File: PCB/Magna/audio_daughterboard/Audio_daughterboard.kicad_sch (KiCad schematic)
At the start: 41 parts, among them J101 Conn_02x15_Odd_Even, U101 CY2305SXC-1HT, U102 CY2305SXC-1HT

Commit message: Update schematics to Kicad 9
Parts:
- U101: LCSC C914887 -> CY2305
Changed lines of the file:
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@@
 	(wire
 		(pts
-			(xy 59.69 74.93) (xy 83.82 74.93)
+			(xy 196.85 71.12) (xy 196.85 90.17)
 		)
 		(stroke
@@
 	(wire
 		(pts
-			(xy 196.85 71.12) (xy 196.85 90.17)
+			(xy 176.53 82.55) (xy 234.95 82.55)
 		)
 		(stroke
@@
 	(wire
 		(pts
-			(xy 176.53 82.55) (xy 234.95 82.55)
+			(xy 288.29 257.81) (xy 288.29 260.35)
 		)
 		(stroke
@@
 	(wire
 		(pts
-			(xy 288.29 257.81) (xy 288.29 260.35)
+			(xy 87.63 52.07) (xy 59.69 52.07)
 		)
 		(stroke
@@
 	(wire
 		(pts
-			(xy 87.63 52.07) (xy 59.69 52.07)
+			(xy 293.37 210.82) (xy 344.17 210.82)
 		)
 		(stroke
@@
 	(wire
 		(pts
-			(xy 293.37 210.82) (xy 344.17 210.82)
+			(xy 379.73 30.48) (xy 379.73 81.28)
 		)
 		(stroke
@@
 	(wire
 		(pts
-			(xy 379.73 30.48) (xy 379.73 81.28)
+			(xy 163.83 74.93) (xy 163.83 77.47)
 		)
 		(stroke
@@
 	(wire
 		(pts
-			(xy 163.83 74.93) (xy 163.83 77.47)
+			(xy 59.69 74.93) (xy 83.82 74.93)
 		)
 		(stroke
@@
 					(size 1.27 1.27)
 				)
+				(hide yes)
 			)
 		)
@@
 					(size 1.27 1.27)
 				)
+				(hide yes)
 			)
 		)
@@
 					(size 1.27 1.27)
 				)
+				(hide yes)
 			)
 		)
@@
 					(size 1.27 1.27)
 				)
+				(hide yes)
 			)
 		)
@@
 					(size 1.27 1.27)
 				)
+				(hide yes)
 			)
 		)
@@
 					(size 1.27 1.27)
 				)
+				(hide yes)
 			)
 		)
@@
 					(size 1.27 1.27)
 				)
+				(hide yes)
 			)
 		)
@@
 					(size 1.27 1.27)
 				)
+				(hide yes)
 			)
 		)
@@
 					(size 1.27 1.27)
 				)
+				(hide yes)
 			)
 		)
@@
 					(size 1.27 1.27)
 				)
+				(hide yes)
 			)
 		)
@@
 					(size 1.27 1.27)
 				)
+				(hide yes)
 			)
 		)
@@
 					(size 1.27 1.27)
 				)
+				(hide yes)
 			)
 		)
@@
 					(size 1.27 1.27)
 				)
+				(hide yes)
 			)
 		)
@@
 					(size 1.27 1.27)
 				)
+				(hide yes)
 			)
 		)
@@
 					(size 1.27 1.27)
 				)
+				(hide yes)
 			)
 		)
@@
 					(size 1.27 1.27)
 				)
+				(hide yes)
 			)
 		)
@@
 					(size 1.27 1.27)
 				)
+				(hide yes)
 			)
 		)
@@
 					(size 1.27 1.27)
 				)
+				(hide yes)
 			)
 		)
@@
 					(size 1.27 1.27)
 				)
+				(hide yes)
 			)
 		)
@@
 					(size 1.27 1.27)
 				)
+				(hide yes)
 			)
 		)
@@
 					(size 1.27 1.27)
 				)
+				(hide yes)
 			)
 		)
@@
 					(size 1.27 1.27)
 				)
+				(hide yes)
 			)
 		)
@@
 					(size 1.27 1.27)
 				)
+				(hide yes)
 			)
 		)
@@
 					(size 1.27 1.27)
 				)
+				(hide yes)
 			)
 		)
@@
 					(size 1.27 1.27)
 				)
+				(hide yes)
 			)
 		)
@@
 					(size 1.27 1.27)
 				)
+				(hide yes)
 			)
 		)
@@
 					(size 1.27 1.27)
 				)
+				(hide yes)
 			)
 		)
@@
 					(size 1.27 1.27)
 				)
+				(hide yes)
 			)
 		)
@@
 					(size 1.27 1.27)
 				)
+				(hide yes)
 			)
 		)
@@
 					(size 1.27 1.27)
 				)
+				(hide yes)
 			)
 		)
@@
 					(size 1.27 1.27)
 				)
+				(hide yes)
 			)
 		)
@@
 					(size 1.27 1.27)
 				)
+				(hide yes)
 			)
 		)
@@
 					(size 1.27 1.27)
 				)
+				(hide yes)
 			)
 		)
@@
 					(size 1.27 1.27)
 				)
+				(hide yes)
 			)
 		)
@@
 					(size 1.27 1.27)
 				)
+				(hide yes)
 			)
 		)
@@
 					(size 1.27 1.27)
 				)
+				(hide yes)
 			)
 		)
@@
 					(size 1.27 1.27)
 				)
+				(hide yes)
 			)
 		)
@@
 					(size 1.27 1.27)
 				)
+				(hide yes)
 			)
 		)
@@
 					(size 1.27 1.27)
 				)
+				(hide yes)
 			)
 		)
@@
 					(size 1.27 1.27)
 				)
+				(hide yes)
 			)
 		)
@@
 					(size 1.27 1.27)
 				)
+				(hide yes)
 			)
 		)
@@
 					(size 1.27 1.27)
 				)
+				(hide yes)
 			)
 		)
@@
 					(size 1.27 1.27)
 				)
+				(hide yes)
 			)
 		)
@@
 					(size 1.27 1.27)
 				)
+				(hide yes)
 			)
 		)
@@
 					(size 1.27 1.27)
 				)
+				(hide yes)
 			)
 		)
@@
 					(size 1.27 1.27)
 				)
+				(hide yes)
 			)
 		)
@@
 					(size 1.27 1.27)
 				)
+				(hide yes)
 			)
 		)
@@
 					(size 1.27 1.27)
 				)
+				(hide yes)
 			)
 		)
@@
 					(size 1.27 1.27)
 				)
+				(hide yes)
 			)
 		)
@@
 					(size 1.27 1.27)
 				)
+				(hide yes)
 			)
 		)
@@
 					(size 1.27 1.27)
 				)
+				(hide yes)
 			)
 		)
@@
 					(size 1.27 1.27)
 				)
+				(hide yes)
 			)
 		)
@@
 					(size 1.27 1.27)
 				)
+				(hide yes)
 			)
 		)
@@
 					(size 1.27 1.27)
 				)
+				(hide yes)
 			)
 		)
@@
 					(size 1.27 1.27)
 				)
+				(hide yes)
 			)
 		)
@@
 					(size 1.27 1.27)
 				)
+				(hide yes)
 			)
 		)
@@
 					(size 1.27 1.27)
 				)
+				(hide yes)
 			)
 		)
@@
 					(size 1.27 1.27)
 				)
+				(hide yes)
 			)
 		)
@@
 					(size 1.27 1.27)
 				)
+				(hide yes)
 			)
 		)
@@
 		(at 163.83 87.63 0)
 		(unit 1)
-		(exclude_from_sim yes)
+		(exclude_from_sim no)
 		(in_bom yes)
 		(on_board yes)
@@
 		(fields_autoplaced yes)
 		(property "Reference" "U101"
-			(at 165.8494 76.361 0)
+			(at 165.9733 75.9163 0)
 			(effects
 				(font
@@
 		)
 		(property "Value" "CY2305SXC-1HT"
-			(at 165.8494 78.8979 0)
+			(at 165.9733 78.3406 0)
 			(effects
 				(font
@@
 		)
 		(property "Footprint" "Package_SO:SOIC-8_3.9x4.9mm_P1.27mm"
-			(at 163.83 87.63 0)
+			(at 163.83 85.09 0)
 			(effects
 				(font
@@
 		)
 		(property "Datasheet" "https://datasheet.lcsc.com/lcsc/2011101039_Cypress-Semicon-CY2305SXC-1HT_C914887.pdf"
-			(at 163.83 87.63 0)
+			(at 163.83 90.17 0)
 			(effects
 				(font
@@
 					(size 1.27 1.27)
 				)
+				(hide yes)
 			)
 		)
-		(property "LCSC" "C914887"
+		(property "LCSC" "CY2305"
 			(at 163.83 87.63 0)
 			(effects
@@
 					(size 1.27 1.27)
 				)
+				(hide yes)
 			)
 		)
@@
 					(size 1.27 1.27)
 				)
+				(hide yes)
 			)
 		)

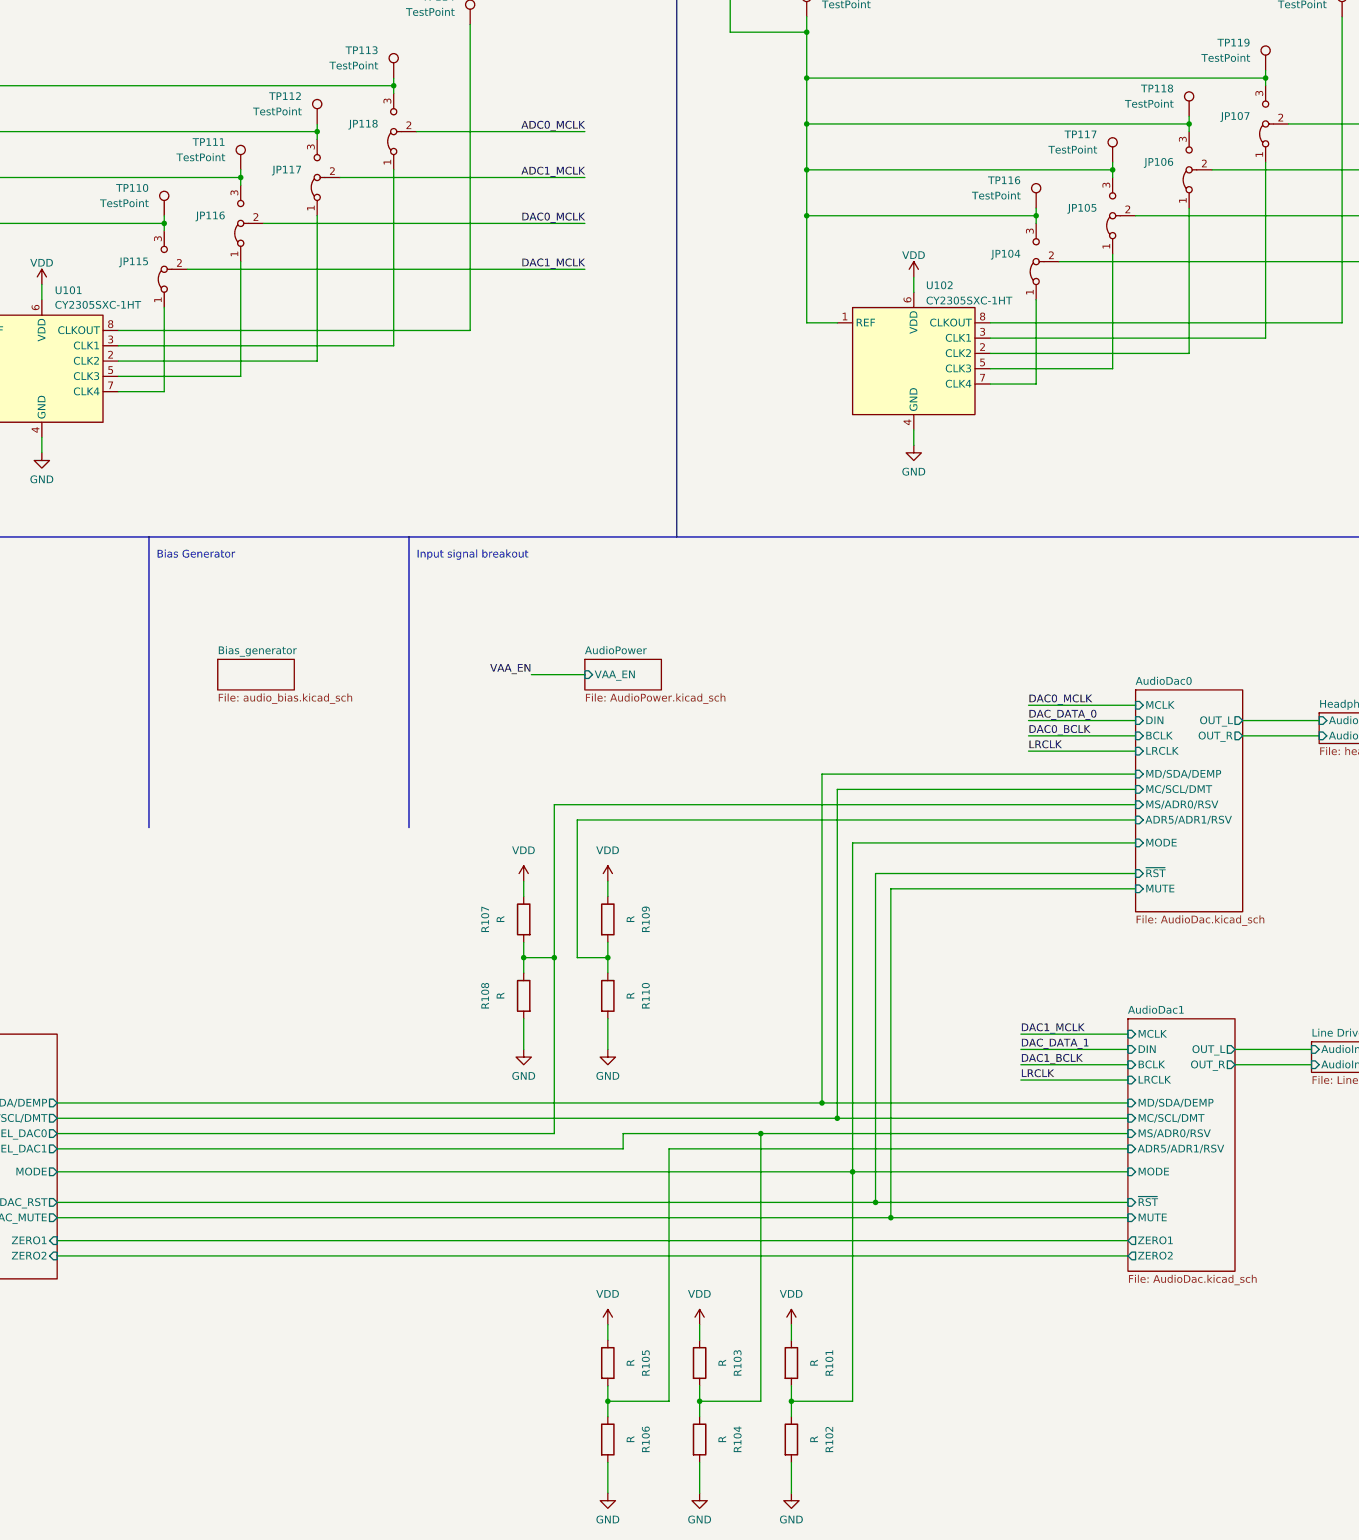
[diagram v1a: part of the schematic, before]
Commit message: Update audio PCB
Mainly added simulations to Linedriver and DAC.

Also fixed some small issues that was found when simulating
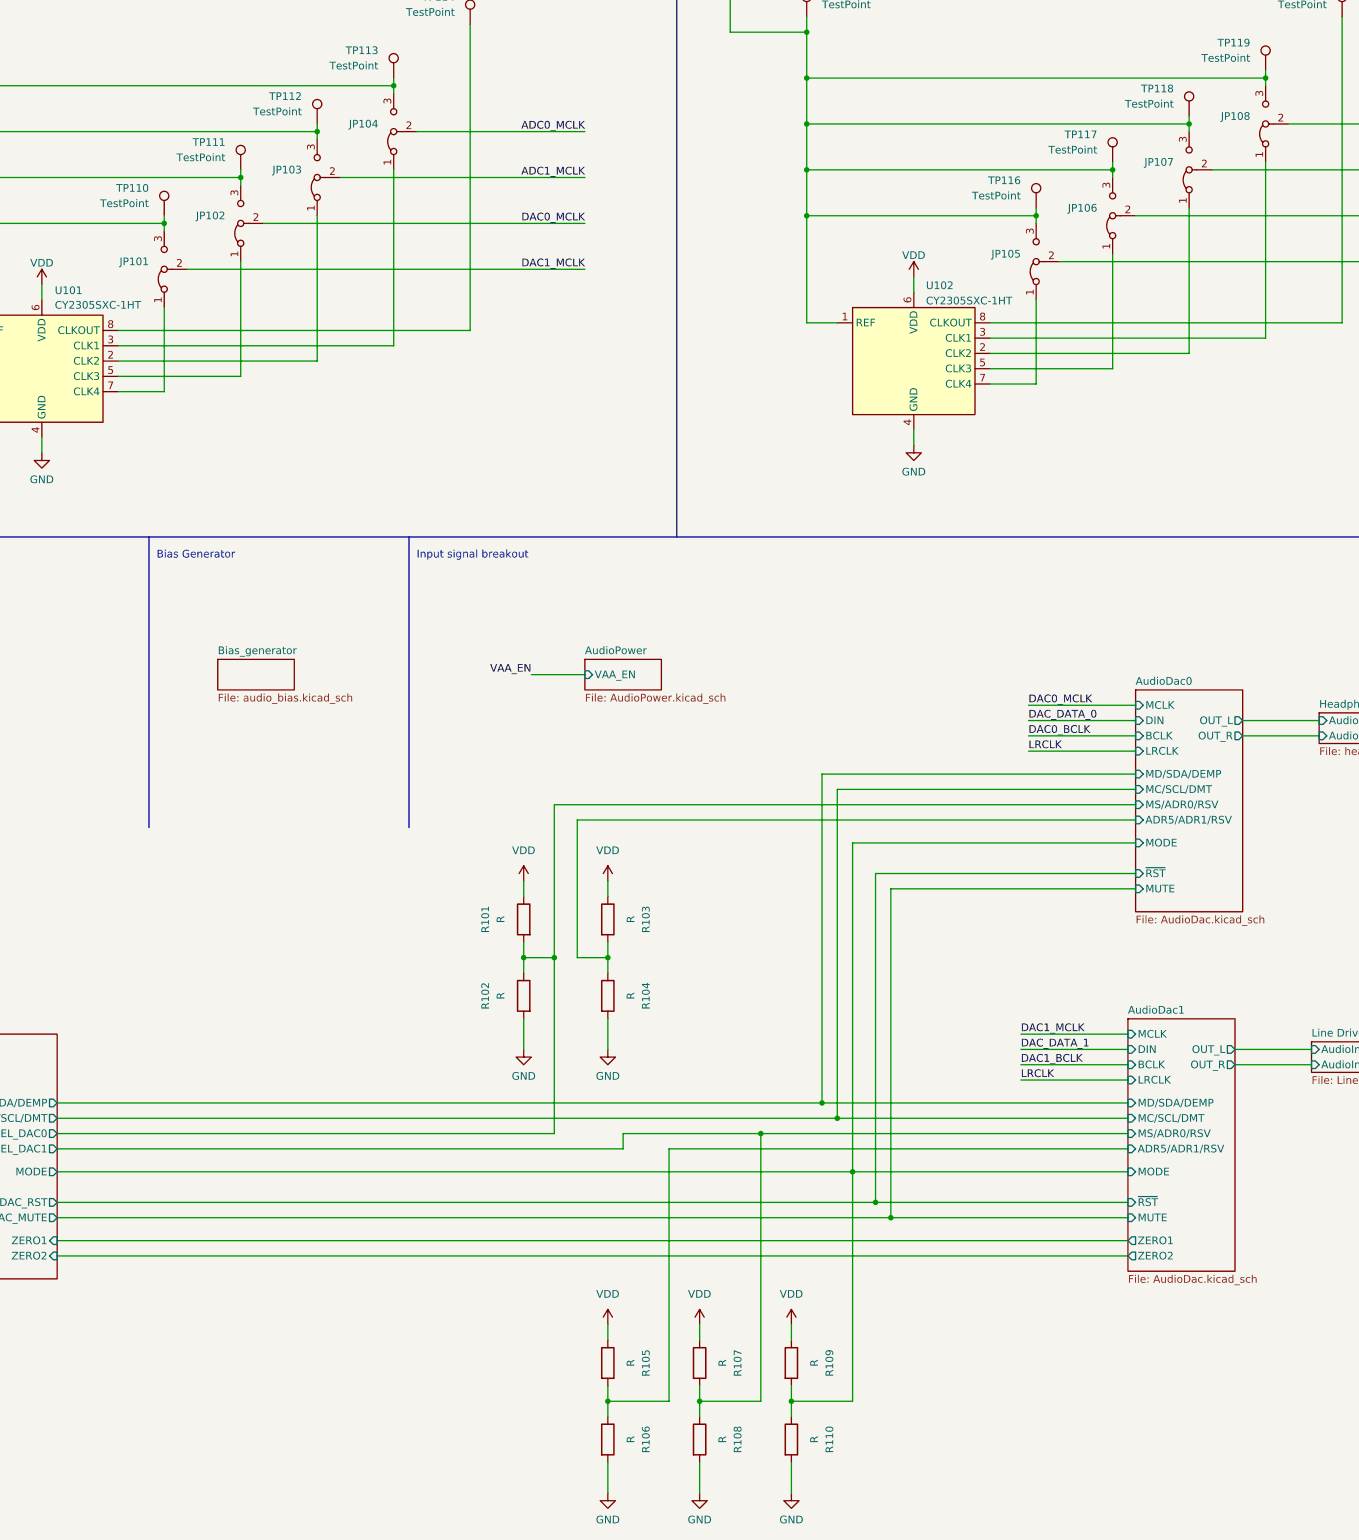
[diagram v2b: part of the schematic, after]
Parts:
- renumbered JP115 to JP101, JP116 to JP102, JP117 to JP103, JP118 to JP104, JP104 to JP105, JP105 to JP106, JP106 to JP107, JP107 to JP108, R107 to R101, R108 to R102, R109 to R103, R110 to R104, R103 to R107, R104 to R108, R101 to R109, R102 to R110

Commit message: "Finalize" Audio daugherboard
Finished DAC output filter
Fixed the whole damn MCU subschematic
Fixed Linedriver schematic
Added component footprints and LCSC numbers
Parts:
- removed R101, R102, R103, R104, R105, R106, R107, R108, R109, R110: R, symbol Device:R
- added R615, R616, R617, R618, R619, R620, R621, R622, R623, R624: 10k, Resistor_SMD:R_0603_1608Metric, symbol Device:R
- JP101, JP102, JP103, JP104, JP105, JP106, JP107, JP108: footprint (none) -> Jumper:SolderJumper-3_P1.3mm_Bridged12_RoundedPad1.0x1.5mm_NumberLabels
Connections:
- net AudioDac0/ADR5/ADR1/RSV: now also R617.2, R618.1
- net AudioDac0/MODE: now also R623.2, R624.1
- net AudioDac0/MS/ADR0/RSV: now also R615.2, R616.1
- net AudioDac1/ADR5/ADR1/RSV: now also R619.2, R620.1
- net AudioDac1/MS/ADR0/RSV: now also R621.2, R622.1
- net GND: now also R616.2, R618.2, R620.2, R622.2, R624.2
- net VAA_EN: no longer J101.29 (Pin_29)
- net VDD: now also R615.1, R617.1, R619.1, R621.1, R623.1
- new net CFG_AUDIO_ENA: J101.29 (Pin_29)
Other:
- sheet AudioDac0 ports: added ZERO1, ZERO2; removed none
- sheet Config MCU ports: added DAC0_ZERO1, DAC0_ZERO2, DAC1_ZERO1, DAC1_ZERO2, MCU_NRST, VAA_ENABLE; removed ZERO1, ZERO2
